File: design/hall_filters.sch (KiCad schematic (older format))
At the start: 11 parts

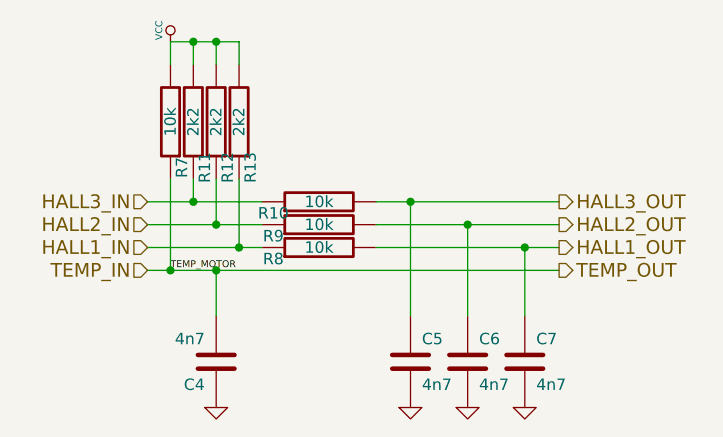
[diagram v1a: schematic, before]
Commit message: Make change in annotations and some small fixes
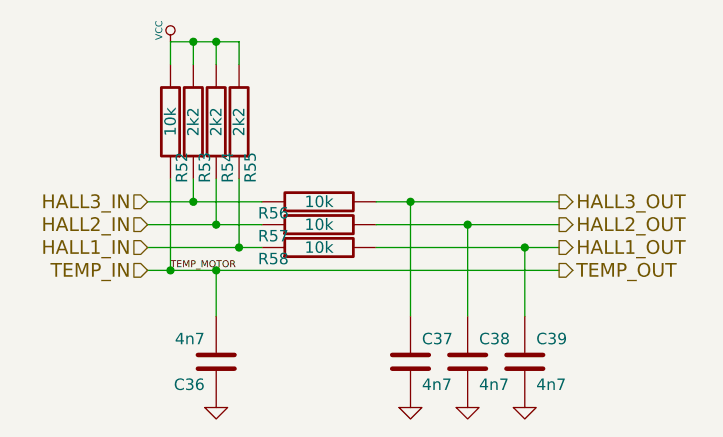
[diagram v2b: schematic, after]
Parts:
- renumbered C4 to C5, C5 to C6, C6 to C7, C7 to C8, R7 to R27, R11 to R28, R12 to R29, R13 to R30, R10 to R31, R9 to R32, R8 to R33
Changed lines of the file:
@@
 $Descr A4 11693 8268
 encoding utf-8
-Sheet 9 11
+Sheet 7 10
 Title ""
-Date "13 jan 2015"
+Date "16 jan 2015"
 Rev ""
 Comp ""
@@
 $EndDescr
 $Comp
-L R R7
+L R R27
 U 1 1 53FBB581
 P 4900 3200
-AR Path="/53FBA77E/53FBB581" Ref="R7"  Part="1"
-AR Path="/54B6AA0D/53FBB581" Ref="R7"  Part="1"
-F 0 "R7" V 4850 3400 50  0000 C CNN
+AR Path="/53FBA77E/53FBB581" Ref="R27"  Part="1"
+AR Path="/54B6AA0D/53FBB581" Ref="R52"  Part="1"
+F 0 "R52" V 4850 3400 50  0000 C CNN
 F 1 "10k" V 4900 3200 50  0000 C CNN
 F 2 "SMD_Packages:SMD-0603_r" H 4900 3200 60  0001 C CNN
@@
 $EndComp
 $Comp
-L R R8
+L R R33
 U 1 1 53FBB588
 P 5550 3750
-AR Path="/53FBA77E/53FBB588" Ref="R8"  Part="1"
-AR Path="/54B6AA0D/53FBB588" Ref="R8"  Part="1"
-F 0 "R8" V 5500 3950 50  0000 C CNN
+AR Path="/53FBA77E/53FBB588" Ref="R33"  Part="1"
+AR Path="/54B6AA0D/53FBB588" Ref="R58"  Part="1"
+F 0 "R58" V 5500 3950 50  0000 C CNN
 F 1 "10k" V 5550 3750 50  0000 C CNN
 F 2 "SMD_Packages:SMD-0603_r" H 5550 3750 60  0001 C CNN
@@
 $EndComp
 $Comp
-L R R9
+L R R32
 U 1 1 53FBB58F
 P 5550 3650
-AR Path="/53FBA77E/53FBB58F" Ref="R9"  Part="1"
-AR Path="/54B6AA0D/53FBB58F" Ref="R9"  Part="1"
-F 0 "R9" V 5500 3850 50  0000 C CNN
+AR Path="/53FBA77E/53FBB58F" Ref="R32"  Part="1"
+AR Path="/54B6AA0D/53FBB58F" Ref="R57"  Part="1"
+F 0 "R57" V 5500 3850 50  0000 C CNN
 F 1 "10k" V 5550 3650 50  0000 C CNN
 F 2 "SMD_Packages:SMD-0603_r" H 5550 3650 60  0001 C CNN
@@
 $EndComp
 $Comp
-L R R10
+L R R31
 U 1 1 53FBB596
 P 5550 3550
-AR Path="/53FBA77E/53FBB596" Ref="R10"  Part="1"
-AR Path="/54B6AA0D/53FBB596" Ref="R10"  Part="1"
-F 0 "R10" V 5500 3750 50  0000 C CNN
+AR Path="/53FBA77E/53FBB596" Ref="R31"  Part="1"
+AR Path="/54B6AA0D/53FBB596" Ref="R56"  Part="1"
+F 0 "R56" V 5500 3750 50  0000 C CNN
 F 1 "10k" V 5550 3550 50  0000 C CNN
 F 2 "SMD_Packages:SMD-0603_r" H 5550 3550 60  0001 C CNN
@@
 $EndComp
 $Comp
-L C C5
+L C C6
 U 1 1 53FBB59D
 P 5950 4250
-AR Path="/53FBA77E/53FBB59D" Ref="C5"  Part="1"
-AR Path="/54B6AA0D/53FBB59D" Ref="C5"  Part="1"
-F 0 "C5" H 6000 4350 50  0000 L CNN
+AR Path="/53FBA77E/53FBB59D" Ref="C6"  Part="1"
+AR Path="/54B6AA0D/53FBB59D" Ref="C37"  Part="1"
+F 0 "C37" H 6000 4350 50  0000 L CNN
 F 1 "4n7" H 6000 4150 50  0000 L CNN
 F 2 "SMD_Packages:SMD-0603_c" H 5950 4250 60  0001 C CNN
@@
 $EndComp
 $Comp
-L C C6
+L C C7
 U 1 1 53FBB5A4
 P 6200 4250
-AR Path="/53FBA77E/53FBB5A4" Ref="C6"  Part="1"
-AR Path="/54B6AA0D/53FBB5A4" Ref="C6"  Part="1"
-F 0 "C6" H 6250 4350 50  0000 L CNN
+AR Path="/53FBA77E/53FBB5A4" Ref="C7"  Part="1"
+AR Path="/54B6AA0D/53FBB5A4" Ref="C38"  Part="1"
+F 0 "C38" H 6250 4350 50  0000 L CNN
 F 1 "4n7" H 6250 4150 50  0000 L CNN
 F 2 "SMD_Packages:SMD-0603_c" H 6200 4250 60  0001 C CNN
@@
 $EndComp
 $Comp
-L C C7
+L C C8
 U 1 1 53FBB5AB
 P 6450 4250
-AR Path="/53FBA77E/53FBB5AB" Ref="C7"  Part="1"
-AR Path="/54B6AA0D/53FBB5AB" Ref="C7"  Part="1"
-F 0 "C7" H 6500 4350 50  0000 L CNN
+AR Path="/53FBA77E/53FBB5AB" Ref="C8"  Part="1"
+AR Path="/54B6AA0D/53FBB5AB" Ref="C39"  Part="1"
+F 0 "C39" H 6500 4350 50  0000 L CNN
 F 1 "4n7" H 6500 4150 50  0000 L CNN
 F 2 "SMD_Packages:SMD-0603_c" H 6450 4250 60  0001 C CNN
@@
 $EndComp
 $Comp
-L GND #PWR030
+L GND #PWR035
 U 1 1 53FBB5B2
 P 5950 4450
-AR Path="/53FBA77E/53FBB5B2" Ref="#PWR030"  Part="1"
-AR Path="/54B6AA0D/53FBB5B2" Ref="#PWR030"  Part="1"
-F 0 "#PWR030" H 5950 4450 30  0001 C CNN
+AR Path="/53FBA77E/53FBB5B2" Ref="#PWR035"  Part="1"
+AR Path="/54B6AA0D/53FBB5B2" Ref="#PWR065"  Part="1"
+F 0 "#PWR065" H 5950 4450 30  0001 C CNN
 F 1 "GND" H 5950 4380 30  0001 C CNN
 F 2 "" H 5950 4450 60  0001 C CNN
@@
 $EndComp
 $Comp
-L R R11
+L R R28
 U 1 1 53FBB5B8
 P 5000 3200
-AR Path="/53FBA77E/53FBB5B8" Ref="R11"  Part="1"
-AR Path="/54B6AA0D/53FBB5B8" Ref="R11"  Part="1"
-F 0 "R11" V 4950 3400 50  0000 C CNN
+AR Path="/53FBA77E/53FBB5B8" Ref="R28"  Part="1"
+AR Path="/54B6AA0D/53FBB5B8" Ref="R53"  Part="1"
+F 0 "R53" V 4950 3400 50  0000 C CNN
 F 1 "2k2" V 5000 3200 50  0000 C CNN
 F 2 "SMD_Packages:SMD-0603_r" H 5000 3200 60  0001 C CNN
@@
 $EndComp
 $Comp
-L R R12
+L R R29
 U 1 1 53FBB5BF
 P 5100 3200
-AR Path="/53FBA77E/53FBB5BF" Ref="R12"  Part="1"
-AR Path="/54B6AA0D/53FBB5BF" Ref="R12"  Part="1"
-F 0 "R12" V 5050 3400 50  0000 C CNN
+AR Path="/53FBA77E/53FBB5BF" Ref="R29"  Part="1"
+AR Path="/54B6AA0D/53FBB5BF" Ref="R54"  Part="1"
+F 0 "R54" V 5050 3400 50  0000 C CNN
 F 1 "2k2" V 5100 3200 50  0000 C CNN
 F 2 "SMD_Packages:SMD-0603_r" H 5100 3200 60  0001 C CNN
@@
 $EndComp
 $Comp
-L R R13
+L R R30
 U 1 1 53FBB5C6
 P 5200 3200
-AR Path="/53FBA77E/53FBB5C6" Ref="R13"  Part="1"
-AR Path="/54B6AA0D/53FBB5C6" Ref="R13"  Part="1"
-F 0 "R13" V 5150 3400 50  0000 C CNN
+AR Path="/53FBA77E/53FBB5C6" Ref="R30"  Part="1"
+AR Path="/54B6AA0D/53FBB5C6" Ref="R55"  Part="1"
+F 0 "R55" V 5150 3400 50  0000 C CNN
 F 1 "2k2" V 5200 3200 50  0000 C CNN
 F 2 "SMD_Packages:SMD-0603_r" H 5200 3200 60  0001 C CNN
@@
 $EndComp
 $Comp
-L C C4
+L C C5
 U 1 1 53FBB5CD
 P 5100 4250
-AR Path="/53FBA77E/53FBB5CD" Ref="C4"  Part="1"
-AR Path="/54B6AA0D/53FBB5CD" Ref="C4"  Part="1"
-F 0 "C4" H 5150 4350 50  0000 L CNN
+AR Path="/53FBA77E/53FBB5CD" Ref="C5"  Part="1"
+AR Path="/54B6AA0D/53FBB5CD" Ref="C36"  Part="1"
+F 0 "C36" H 5150 4350 50  0000 L CNN
 F 1 "4n7" H 5150 4150 50  0000 L CNN
 F 2 "SMD_Packages:SMD-0603_c" H 5100 4250 60  0001 C CNN
@@
 $EndComp
 $Comp
-L GND #PWR031
+L GND #PWR036
 U 1 1 53FBB5D4
 P 5100 4450
-AR Path="/53FBA77E/53FBB5D4" Ref="#PWR031"  Part="1"
-AR Path="/54B6AA0D/53FBB5D4" Ref="#PWR031"  Part="1"
-F 0 "#PWR031" H 5100 4450 30  0001 C CNN
+AR Path="/53FBA77E/53FBB5D4" Ref="#PWR036"  Part="1"
+AR Path="/54B6AA0D/53FBB5D4" Ref="#PWR066"  Part="1"
+F 0 "#PWR066" H 5100 4450 30  0001 C CNN
 F 1 "GND" H 5100 4380 30  0001 C CNN
 F 2 "" H 5100 4450 60  0001 C CNN
@@
 $EndComp
 $Comp
-L VCC #PWR032
+L VCC #PWR037
 U 1 1 53FBB5DA
 P 4900 2850
-AR Path="/53FBA77E/53FBB5DA" Ref="#PWR032"  Part="1"
-AR Path="/54B6AA0D/53FBB5DA" Ref="#PWR032"  Part="1"
-F 0 "#PWR032" H 4900 2950 30  0001 C CNN
+AR Path="/53FBA77E/53FBB5DA" Ref="#PWR037"  Part="1"
+AR Path="/54B6AA0D/53FBB5DA" Ref="#PWR067"  Part="1"
+F 0 "#PWR067" H 4900 2950 30  0001 C CNN
 F 1 "VCC" V 4850 2900 30  0000 C CNN
 F 2 "" H 4900 2850 60  0001 C CNN
@@
 	5100 3850 5100 4050
 $Comp
-L GND #PWR033
+L GND #PWR038
 U 1 1 53FBB5F9
 P 6200 4450
-AR Path="/53FBA77E/53FBB5F9" Ref="#PWR033"  Part="1"
-AR Path="/54B6AA0D/53FBB5F9" Ref="#PWR033"  Part="1"
-F 0 "#PWR033" H 6200 4450 30  0001 C CNN
+AR Path="/53FBA77E/53FBB5F9" Ref="#PWR038"  Part="1"
+AR Path="/54B6AA0D/53FBB5F9" Ref="#PWR068"  Part="1"
+F 0 "#PWR068" H 6200 4450 30  0001 C CNN
 F 1 "GND" H 6200 4380 30  0001 C CNN
 F 2 "" H 6200 4450 60  0001 C CNN
@@
 $EndComp
 $Comp
-L GND #PWR034
+L GND #PWR039
 U 1 1 53FBB5FF
 P 6450 4450
-AR Path="/53FBA77E/53FBB5FF" Ref="#PWR034"  Part="1"
-AR Path="/54B6AA0D/53FBB5FF" Ref="#PWR034"  Part="1"
-F 0 "#PWR034" H 6450 4450 30  0001 C CNN
+AR Path="/53FBA77E/53FBB5FF" Ref="#PWR039"  Part="1"
+AR Path="/54B6AA0D/53FBB5FF" Ref="#PWR069"  Part="1"
+F 0 "#PWR069" H 6450 4450 30  0001 C CNN
 F 1 "GND" H 6450 4380 30  0001 C CNN
 F 2 "" H 6450 4450 60  0001 C CNN
